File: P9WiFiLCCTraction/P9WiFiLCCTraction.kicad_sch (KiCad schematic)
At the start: 31 parts, among them IC102 MP6614GN-Z, J101 USB_C_Receptacle, J102 DCC 9-pin, SW101 Reset, SW102 Boot, U101 ESP32_S3_WROOM, U102 TBD62064AFG_1, U103 AP63203WU

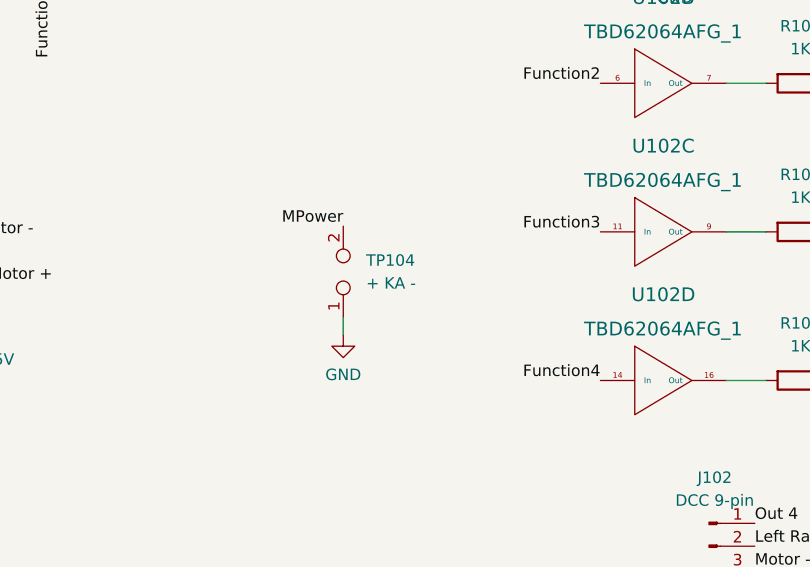
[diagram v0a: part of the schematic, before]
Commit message: Finalize the board (3D models, adjust text.
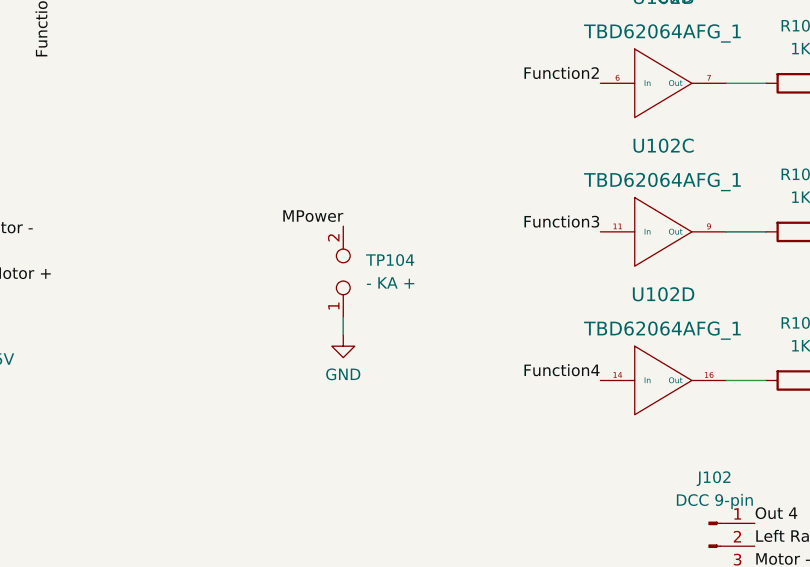
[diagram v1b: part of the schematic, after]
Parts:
- TP104: value + KA - -> - KA +
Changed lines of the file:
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@@
       (effects (font (size 1.27 1.27)) (justify right))
     )
-    (property "Value" "+ KA -" (id 1) (at 113.03 110.4899 90)
+    (property "Value" "- KA +" (id 1) (at 113.03 110.4899 90)
       (effects (font (size 1.27 1.27)) (justify right))
     )
@@
     )
     (path "/3032618d-7173-4140-8b2d-ca8a6623fcee"
-      (reference "TP104") (unit 1) (value "+ KA -") (footprint "TestPoint:TestPoint_2Pads_Pitch2.54mm_Drill0.8mm")
+      (reference "TP104") (unit 1) (value "- KA +") (footprint "TestPoint:TestPoint_2Pads_Pitch2.54mm_Drill0.8mm")
     )
     (path "/9724c26f-89b9-4862-8667-a2ad7abdb7a0"

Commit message: Add README and Schematic.
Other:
- company: (none) -> Deepwoods Software
- title: (none) -> JST 9-Pin WiFi LCC Traction Node
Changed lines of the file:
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@@
 (kicad_sch (version 20211123) (generator eeschema)
-  (paper "A4")
+  (paper "USLetter")
+  (title_block
+    (title "JST 9-Pin WiFi LCC Traction Node")
+    (date "12/11/2025")
+    (rev "A")
+    (company "Deepwoods Software")
+  )
   (junction (at 42.545 158.75) (diameter 0) (color 0 0 0 0)
   )

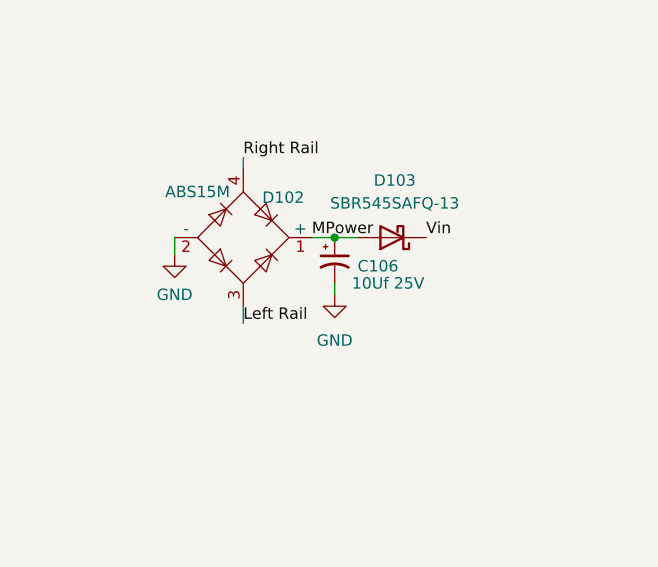
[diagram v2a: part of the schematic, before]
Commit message: Increase Cap. on power supply.
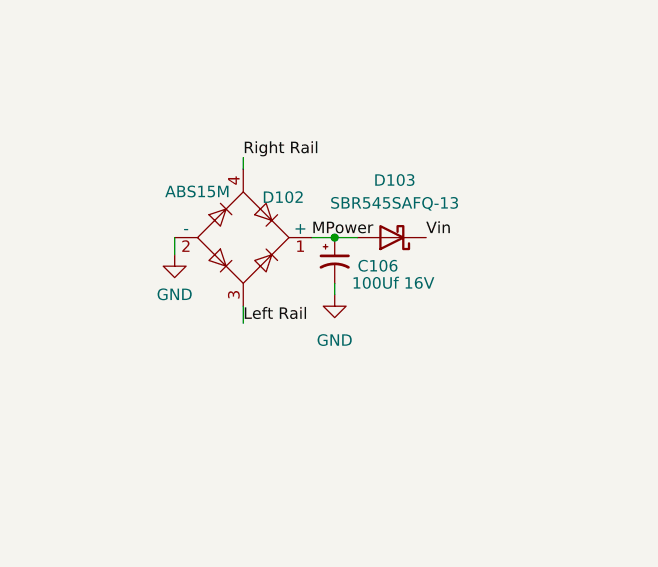
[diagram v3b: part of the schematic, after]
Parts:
- C106: value 10Uf 25V -> 100Uf 16V; Manufacturer_Name KEMET -> KYOCERA AVX; Manufacturer_Part_Number T491C106K025AT7280 -> F931C107MCC; Mouser Part Number 80-T491C106K25AT7280 -> 647-F931C107MCC
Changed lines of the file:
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@@
       (effects (font (size 1.27 1.27)) (justify left))
     )
-    (property "Value" "10Uf 25V" (id 1) (at 230.505 132.715 0)
+    (property "Value" "100Uf 16V" (id 1) (at 230.505 132.715 0)
       (effects (font (size 1.27 1.27)) (justify left))
     )
@@
       (effects (font (size 1.27 1.27)) hide)
     )
-    (property "Mouser Part Number" "80-T491C106K25AT7280" (id 4) (at 228.6 130.175 0)
-      (effects (font (size 1.27 1.27)) hide)
-    )
-    (property "Manufacturer_Name" "KEMET" (id 5) (at 26.67 -694.92 0)
-      (effects (font (size 1.27 1.27)) (justify left top) hide)
-    )
-    (property "Manufacturer_Part_Number" "T491C106K025AT7280" (id 6) (at 26.67 -794.92 0)
+    (property "Mouser Part Number" "647-F931C107MCC" (id 4) (at 228.6 130.175 0)
+      (effects (font (size 1.27 1.27)) hide)
+    )
+    (property "Manufacturer_Name" "KYOCERA AVX" (id 5) (at 26.67 -694.92 0)
+      (effects (font (size 1.27 1.27)) (justify left top) hide)
+    )
+    (property "Manufacturer_Part_Number" "F931C107MCC" (id 6) (at 26.67 -794.92 0)
       (effects (font (size 1.27 1.27)) (justify left top) hide)
     )
@@
     )
     (path "/7ed8c76b-a32b-44f1-b7ad-61c8b65583b5"
-      (reference "C106") (unit 1) (value "10Uf 25V") (footprint "Capacitor_Tantalum_SMD:CP_EIA-6032-28_Kemet-C")
+      (reference "C106") (unit 1) (value "100Uf 16V") (footprint "Capacitor_Tantalum_SMD:CP_EIA-6032-28_Kemet-C")
     )
     (path "/f2670815-23fc-49e4-8b97-c6f0855c0d37"
